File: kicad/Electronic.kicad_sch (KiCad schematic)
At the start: 12 parts, among them J1 BATT, J2 SOLAR, J3 US1881, Q1 IRLZ44N, U1 WEMOS_D1_mini, U3 MCP1700x-330xxTO

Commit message: v386 : electronic schematic update
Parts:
- removed U1: WEMOS_D1_mini, RF_Module:WEMOS_D1_mini_light, symbol RF_Module:WEMOS_D1_mini
- added U1: WeMos_mini, wemos_d1_mini:D1_mini_board, symbol wemos_mini:WeMos_mini
- C1: footprint Capacitor_THT:C_Disc_D10.0mm_W2.5mm_P5.00mm -> Capacitor_THT:C_Disc_D3.0mm_W2.0mm_P2.50mm
- C2: footprint Capacitor_THT:CP_Radial_D10.0mm_P2.50mm -> Capacitor_THT:CP_Radial_D4.0mm_P2.00mm
- J1: value BATT -> BAT; footprint (none) -> Connector_PinHeader_2.00mm:PinHeader_1x02_P2.00mm_Vertical
- J2: value SOLAR -> SOL; footprint (none) -> Connector_PinHeader_2.00mm:PinHeader_1x02_P2.00mm_Vertical
- J3: footprint (none) -> Connector_PinHeader_2.00mm:PinHeader_1x03_P2.00mm_Vertical
- R1: footprint Resistor_THT:R_Axial_DIN0411_L9.9mm_D3.6mm_P25.40mm_Horizontal -> Resistor_THT:R_Axial_DIN0309_L9.0mm_D3.2mm_P12.70mm_Horizontal
- R2, R3: footprint (none) -> Resistor_THT:R_Axial_DIN0309_L9.0mm_D3.2mm_P12.70mm_Horizontal
- TP1: footprint (none) -> tp4056_usb_c_module:TP4056_module
- U2: renamed from U3; value MCP1700x-330xxTO -> MCP1700-330
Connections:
- net GND: now also U1.2 (GND)
- net +SOL: now reaches J2.1 (Pin_1), TP1.1 (5V+)
- net -SOL: now reaches J2.2 (Pin_2), TP1.2 (-)
- net +BAT: now reaches TP1.5 (OUT+), U2.2 (VI)
- net +BAT: now also J1.1 (Pin_1), R1.1, TP1.3 (B+)
- net 3.3V: now reaches C1.1, C2.1, J3.1 (Pin_1), U2.3 (VO)
- net 3.3V: now also U1.16 (3.3V)
- net at R2.1: now also U1.12 (D5)
- net -BAT: now reaches J1.2 (Pin_2), TP1.4 (B-)
- net -OUT: now reaches J3.2 (Pin_2), Q1.2 (D)
- net VIT: now reaches J3.3 (Pin_3)
- net VIT: now also U1.13 (D6)
- net at R1.2: now also U1.10 (A0)
- new net: U1.11 (D0), U1.9 (Rst)
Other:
- moved on the sheet: C1, C2, R1

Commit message: v386 : electronic schematic update
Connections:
- net +BAT: no longer TP1.5 (OUT+), U2.2 (VI)
- new net +VR: TP1.5 (OUT+), U2.2 (VI)
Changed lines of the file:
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@@
 		)
 	)
-	(label "+BAT"
+	(label "+VR"
 		(at 87.63 82.55 0)
 		(effects

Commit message: v386 : electronic schematic update
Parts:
- removed J3: US1881, Connector_PinHeader_2.00mm:PinHeader_1x03_P2.00mm_Vertical, symbol Connector:Conn_01x03_Pin
- added J3: ANM, Connector_JST:JST_PH_B5B-PH-K_1x05_P2.00mm_Vertical, symbol Connector:Conn_01x05_Pin
- added J4: GIR, Connector_JST:JST_PH_B5B-PH-K_1x05_P2.00mm_Vertical, symbol Connector:Conn_01x05_Pin
- added J5: SERIAL, Connector_PinHeader_2.54mm:PinHeader_1x02_P2.54mm_Vertical, symbol Connector:Conn_01x02_Pin
- C2: footprint Capacitor_THT:CP_Radial_D4.0mm_P2.00mm -> Capacitor_THT:CP_Radial_D6.3mm_P2.50mm
- J1: footprint Connector_PinHeader_2.00mm:PinHeader_1x02_P2.00mm_Vertical -> Connector_JST:JST_XH_B2B-XH-A_1x02_P2.50mm_Vertical
- J2: footprint Connector_PinHeader_2.00mm:PinHeader_1x02_P2.00mm_Vertical -> Connector_JST:JST_PH_B2B-PH-K_1x02_P2.00mm_Vertical
- R1, R3: footprint Resistor_THT:R_Axial_DIN0309_L9.0mm_D3.2mm_P12.70mm_Horizontal -> Resistor_THT:R_Axial_DIN0414_L11.9mm_D4.5mm_P15.24mm_Horizontal
- R2: value 220 -> 330; footprint Resistor_THT:R_Axial_DIN0309_L9.0mm_D3.2mm_P12.70mm_Horizontal -> Resistor_THT:R_Axial_DIN0414_L11.9mm_D4.5mm_P15.24mm_Horizontal
- U1: value WeMos_mini -> WeMos_D1_mini_pro; footprint wemos_d1_mini:D1_mini_board -> RF_Module:WEMOS_D1_mini_light
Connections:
- net +BAT: now also J1.2 (Pin_2); no longer J1.1 (Pin_1)
- net +SOL: now also J2.2 (Pin_2); no longer J2.1 (Pin_1)
- net -BAT: now also J1.1 (Pin_1); no longer J1.2 (Pin_2)
- net -OUT: now also J3.1 (Pin_1), J4.1 (Pin_1)
- net -SOL: now also J2.1 (Pin_1); no longer J2.2 (Pin_2)
- net 3.3V: now also U1.8 (3.3V), J3.2 (Pin_2), J4.2 (Pin_2); no longer U1.16 (3.3V)
- net GND: now also U1.10 (GND); no longer U1.2 (GND)
- net VIT: now also U1.5 (D6), J3.3 (Pin_3); no longer U1.13 (D6)
- net at R2.1: now also U1.4 (D5); no longer U1.12 (D5)
- net at U1.1 (Rst): now also U1.3 (D0)
- net at R1.2: now also U1.2 (A0); no longer U1.10 (A0)
- net at U1.11 (D4): no longer U1.9 (Rst)
- net at U1.14 (D1): now also J4.3 (Pin_3)
- net RX: now reaches U1.15 (Rx)
- net RX: now also J5.2 (Pin_2)
- net at U1.6 (D7): now also J3.4 (Pin_4)
- net at U1.7 (D8): now also J3.5 (Pin_5)
- new net: J4.5 (Pin_5), U1.12 (D3)
- new net: J4.4 (Pin_4), U1.13 (D2)
- new net TX: J5.1 (Pin_1), U1.16 (Tx)

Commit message: v386 : electronic schematic update
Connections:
- net at U1.12 (D3): now also J4.3 (Pin_3); no longer J4.5 (Pin_5)
- net at U1.14 (D1): now also J4.5 (Pin_5); no longer J4.3 (Pin_3)
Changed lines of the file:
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@@
+	(wire
+		(pts
+			(xy 137.16 92.71) (xy 140.97 92.71)
+		)
+		(stroke
+			(width 0)
+			(type default)
+		)
+	)
 	(wire
 		(pts
@@
 	(wire
 		(pts
+			(xy 139.7 87.63) (xy 140.97 87.63)
+		)
+		(stroke
+			(width 0)
+			(type default)
+		)
+	)
+	(wire
+		(pts
 			(xy 194.31 101.6) (xy 194.31 104.14)
 		)
@@
 	(wire
 		(pts
-			(xy 139.7 92.71) (xy 140.97 92.71)
-		)
-		(stroke
-			(width 0)
-			(type default)
-		)
-	)
-	(wire
-		(pts
 			(xy 195.58 58.42) (xy 214.63 58.42)
 		)
@@
 	(wire
 		(pts
-			(xy 139.7 125.73) (xy 139.7 92.71)
+			(xy 139.7 87.63) (xy 139.7 125.73)
 		)
 		(stroke
@@
 	(wire
 		(pts
-			(xy 137.16 87.63) (xy 137.16 130.81)
-		)
-		(stroke
-			(width 0)
-			(type default)
-		)
-	)
-	(wire
-		(pts
 			(xy 190.5 143.51) (xy 217.17 143.51)
 		)
@@
 	(wire
 		(pts
-			(xy 137.16 87.63) (xy 140.97 87.63)
-		)
-		(stroke
-			(width 0)
-			(type default)
-		)
-	)
-	(wire
-		(pts
 			(xy 170.18 95.25) (xy 166.37 95.25)
 		)
@@
 		)
 		(stroke
+			(width 0)
+			(type default)
+		)
+	)
+	(wire
+		(pts
+			(xy 137.16 130.81) (xy 137.16 92.71)
+		)
+		(stroke

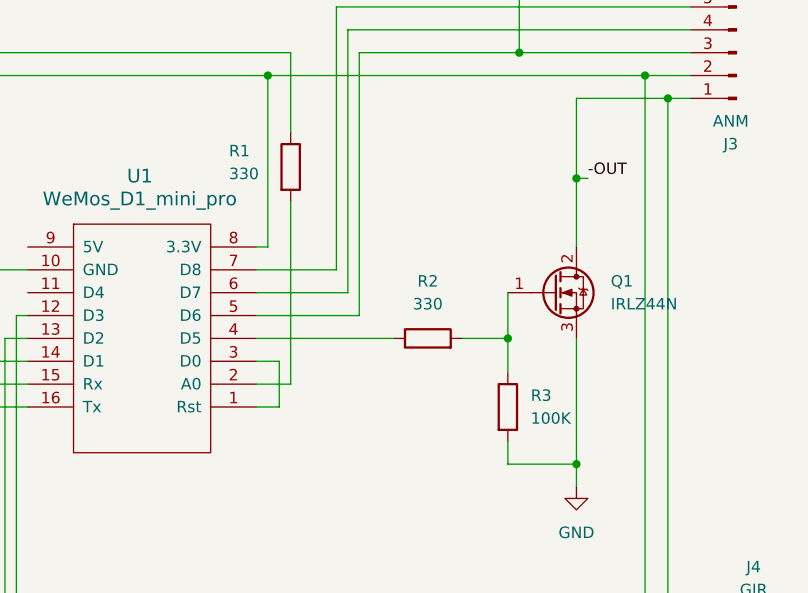
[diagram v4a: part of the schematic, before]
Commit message: v441 : fix resistor values on PCB
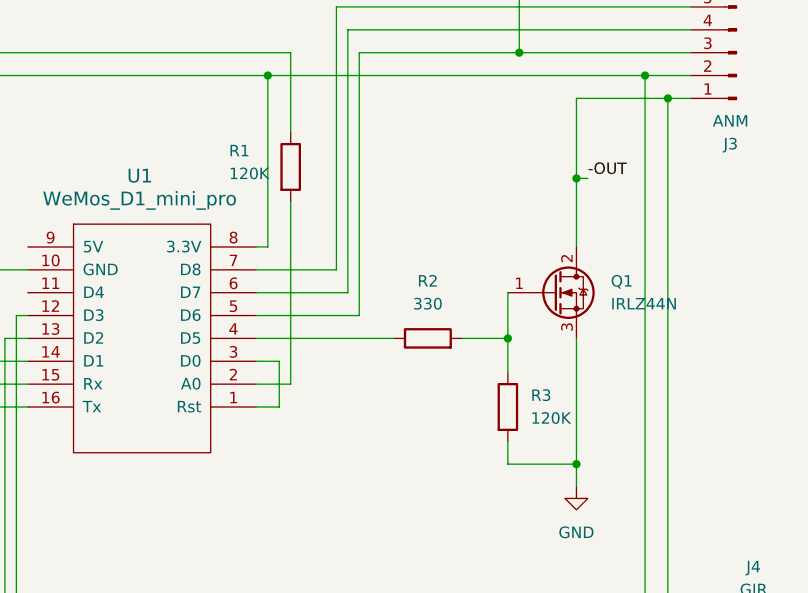
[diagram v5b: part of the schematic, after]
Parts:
- R1: value 330 -> 120K
- R3: value 100K -> 120K
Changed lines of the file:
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@@
 			)
 		)
-		(property "Value" "100K"
+		(property "Value" "120K"
 			(at 196.85 99.0599 0)
 			(show_name no)
@@
 			)
 		)
-		(property "Value" "330"
+		(property "Value" "120K"
 			(at 163.322 71.882 0)
 			(show_name no)
